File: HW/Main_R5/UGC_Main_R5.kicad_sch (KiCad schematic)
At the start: 167 parts, among them J1 SM02B-SURS-TF_LF__SN_, J10 SM02B-SURS-TF_LF__SN_, J13 503480-0640, J2 503480-0640, J4 Conn_01x06_Pin, J5 UJ31-CH-G1-SMT-TR, J6 Trigger, J7 Trigger, J8 Conn_01x02, J9 Conn_01x02, Q1 MMBT3904, Q2 MMBT3904, Q3 BSS138DW, Q4 BSS138DW, Q5 MMBT2222A, Q6 MMBT2222A, SW1 1TS026A-1000-0550, SW1 SW_Push, SW10 SW_Push, SW11 SW_Push, SW12 SW_Push, SW13 SW_Push, SW14 TS-1187A-C-A-B, SW17 TS-1187A-C-A-B, SW18 TS-1187A-C-A-B, SW19 TS-1187A-C-A-B, SW2 SW_Push, SW3 SW_Push, SW4 SW_Push, SW5 TS-1187A-C-A-B, SW6 GL18_SW, SW7 SW_Push, SW8 SW_Push, SW9 TS-1187A-C-A-B, U1 ESP32-PICO-MINI-02, U10 ST_LSM6, U11 BQ25180, U12 CH340K, U13 PI3USB4000A, U2 GD25Q80EEIGR, U4 TPS630001RCR, U5 ST_LSM6, U6 MCP3002, U7 MCP3002, U8 RP2040, X1 ModConnect, X2 ModConnect, X3 ModConnect, X4 ModConnect, X5 ModConnect, X6 ModConnect, Y1 ABM8-272-T3

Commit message: R5 Update
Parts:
- removed C2: 10uF, Capacitor_SMD:C_0805_2012Metric, symbol Device:C
- removed C20, C22: 100nF, Capacitor_SMD:C_0201_0603Metric, symbol Device:C
- removed C21: 1uF, Capacitor_SMD:C_0201_0603Metric, symbol Device:C
- removed Q1, Q2: MMBT3904, Package_TO_SOT_SMD:SOT-23, symbol Transistor_BJT:MMBT3904
- removed R20, R29, R30: 10k, Resistor_SMD:R_0201_0603Metric, symbol Device:R_Small
- removed SW1: 1TS026A-1000-0550, hhl:1TS026A-1000-0550, symbol hhl:1TS026A-1000-0550
- removed U1: ESP32-PICO-MINI-02, hhl:MODULE_ESP32-PICO-MINI-02, symbol hhl:ESP32-PICO-MINI-02
- removed U12: CH340K, hhl:ESSOP-10, symbol hhl:CH340K
- removed U13: PI3USB4000A, Package_DFN_QFN:Texas_UQFN-10_1.5x2mm_P0.5mm, symbol hhl:PI3USB4000AZUAEX
- removed U6, U7: MCP3002, Package_SO:MSOP-8_3x3mm_P0.65mm, symbol Analog_ADC:MCP3002
- added L14, L15, L8, L9: SK6805-EC-15, hhl:SK6805-EC-15, symbol progcc_v3:SK6805-EC-15
- added L7: BLM18AG601SN1D, Inductor_SMD:L_0603_1608Metric, symbol Device:L
- added P1: RPI-RM2, hhl:RPI_RM2, symbol hhl:RPI-RM2
- added S7: TMUX1204DQAR, hhl:TMUX1204DQAR, symbol hhl:TMUX1204DQAR
- added U1, U2, U3: USBLC6-2P6, Package_TO_SOT_SMD:SOT-666, symbol Power_Protection:USBLC6-2P6
- C18: footprint Capacitor_SMD:C_0201_0603Metric -> Capacitor_SMD:C_0402_1005Metric; Confirmed YES -> (none); LCSC C160831 -> C541406; Link https://www.lcsc.com/product-detail/Multilayer-Ceramic-Capa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 -> (none); MPN CL03A104KQ3NNNC -> CC0402KRX7R5BB104; Package 0201 -> 0402
- R16: Confirmed YES -> (none); Link https://www.lcsc.com/product-detail/Chip-Resistor-Surface-M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 -> (none); USBDNP (none) -> YES
- R17: value 10k -> 470R; Confirmed YES -> (none); LCSC C106225 -> C226558; Link https://www.lcsc.com/product-detail/Chip-Resistor-Surface-M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 -> (none); MPN RC0201FR-0710KL -> AC0201FR-07470RL; USBDNP (none) -> YES
- R18, R19: value 0R -> 1k; Confirmed YES -> (none); LCSC C106227 -> C138165; Link https://www.lcsc.com/product-detail/Chip-Resistor-Surface-M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 -> (none); MPN RC0201FR-070RL -> RC0201FR-071KL; Price 0.0005 -> 0.0006
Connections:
- net ESP_IO13 is gone; now on net +3V3: R19.2
- net ESP_IO15 is gone; now on net +3V3: R18.1
- net RADC_CS is gone; now on net LRA_R: U8.12 (GPIO9)
- net USB_EN is gone; now on net I2C0_SDA: U8.36 (GPIO24)
- net USB_SEL is gone; now on net I2C0_SCL: U8.37 (GPIO25)
- net +3V3: now also U10.1 (SDO), U10.12 (CS), U5.12 (CS), L14.2 (VDD), L15.2 (VDD), L7.1, L8.2 (VDD), L9.2 (VDD), S7.5 (EN), S7.6 (VDD)
- net BTN_PWR: now also U8.2 (GPIO0); no longer U8.7 (GPIO5)
- net D+: now also U1.3 (I/O2)
- net D-: now also U1.1 (I/O1)
- net GND: now also U5.1 (SDO), L14.4 (GND), L15.4 (GND), L8.4 (GND), L9.4 (GND), P1.A1 (GND), P1.A4 (GND), P1.A7 (GND), P1.B4 (GND), P1.C1 (GND), P1.C7 (GND), S7.3 (GND), U1.2 (GND), U2.2 (GND), U3.2 (GND)
- net I2C_SCL: no longer R8.2, U8.35 (GPIO23)
- net I2C_SDA: no longer R9.1, U8.34 (GPIO22)
- net LRA_L: now also U8.11 (GPIO8); no longer U8.5 (GPIO3)
- net LRA_R: no longer U8.11 (GPIO8)
- net LX: now also S7.4 (S3)
- net LY: now also S7.2 (S1)
- net N_CLOCK: now also U2.4 (I/O2); no longer Q4.6 (D1), R27.2
- net N_DATA: now also U3.6 (I/O1); no longer Q4.4 (S2), R28.2
- net N_LATCH: now also U2.6 (I/O1); no longer Q3.4 (S2), R26.2
- net RX: now also S7.7 (S4)
- net RY: now also S7.9 (S2)
- net WL_D: now reaches R16.2
- net WL_D: now also R17.1, U8.5 (GPIO3), P1.A5 (DI)
- net ESP_CTS renamed I2C0_SCL
- net I2C0_SCL: now also U10.13 (SCL), U5.13 (SCL)
- net ESP_DTR: no longer names the net of R16.1
- net ESP_DTR: now also P1.B3 (IRQ)
- net ESP_EN renamed ADC_MUX_OUT
- net ADC_MUX_OUT: now also S7.8 (D)
- net ESP_RTS: no longer names the net of R17.2
- net ESP_RTS: now also P1.A6 (DO); no longer R19.1
- removed net IMU0_CS: U10.12 (CS), U8.2 (GPIO0)
- net IMU1_CS renamed WL_ON
- net WL_ON: now also P1.B5 (WLON), P1.B6 (BTON); no longer U5.12 (CS)
- net LADC_CS: no longer names the net of U8.3 (GPIO1)
- net PLAYER_RGB: no longer names the net of L6.1 (DIN)
- net PLAYER_RGB: now also L15.3 (DOUT); no longer L4.3 (DOUT)
- net RP_USB+ renamed SAFE_D+
- net SAFE_D+: now also U1.4 (I/O2)
- net RP_USB- renamed SAFE_D-
- net SAFE_D-: now also U1.6 (I/O1)
- removed net SPI_CK: U10.13 (SCL), U5.13 (SCL), U8.8 (GPIO6)
- removed net SPI_RX: U10.1 (SDO), U5.1 (SDO), U8.6 (GPIO4)
- net SPI_TX renamed I2C0_SDA
- net I2C0_SDA: now also R19.1; no longer U8.9 (GPIO7)
- new net: L8.3 (DOUT), L9.1 (DIN)
- new net: L14.3 (DOUT), L15.1 (DIN)
- new net: L14.1 (DIN), L9.3 (DOUT)
- new net +3.3V_PRE: U3.5 (VBUS)
- new net ADC_ADDR_0: S7.1 (A0)
- new net ADC_ADDR_1: S7.10 (A1)
- new net DPAD_RGB: L4.3 (DOUT), L8.1 (DIN)
- new net I2C1_SCL: R8.2, U8.35 (GPIO23)
- new net I2C1_SDA: R9.1, U8.34 (GPIO22)
- new net N_CLOCK_SAFE: Q4.6 (D1), R27.2, U2.3 (I/O2)
- new net N_DATA_SAFE: Q4.4 (S2), R28.2, U3.1 (I/O1)
- new net N_LATCH_SAFE: Q3.4 (S2), R26.2, U2.1 (I/O1)
- new net VBUS_PRE: U1.5 (VBUS)
- new net VDDBAT: L7.2, P1.B7 (VDDIO), P1.C2 (VDDBAT)
- new net WL_CLK: P1.A3 (SCLK), U8.6 (GPIO4)
- new net WL_CS: P1.B2 (CS), U8.7 (GPIO5)
- new net WL_GP0: P1.B1 (GPIO0)
- new net WL_GP1: P1.C4 (GPIO1)
- new net WL_GP2: P1.C3 (GPIO2)
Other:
- note added: "Analog Mux"
- note added: "ESD"
- note added: "RPI-RM2 Wireless"
- note removed: "ADCs"
- note removed: "ESP32 EN Pullup"
- note removed: "ESP32 Pico Mini 02"
- note removed: "ESP32 UART Bridge IC"
- note removed: "USB Switch"
- moved on the sheet: C1, C12, C13, C2, J13, J4, L10, L11, L12, L13, L6, R1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

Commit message: More routing
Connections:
- net +3.3V_PRE is gone; now on net +3V3_PRE: U3.5 (VBUS)
- net I2C_SCL is gone; now on net I2C1_SCL: U11.B1 (SCL)
- net I2C_SDA is gone; now on net I2C1_SDA: U11.C1 (SDA)
- net VBUS_PRE is gone; now on net +5V_PRE: U1.5 (VBUS)
- net ADC_ADDR_0: now also U8.6 (GPIO4)
- net ADC_ADDR_1: now also U8.7 (GPIO5)
- net ADC_MUX_OUT: now also U8.41 (GPIO29_ADC3); no longer U8.38 (GPIO26_ADC0)
- net BTN_PWR: now also U8.8 (GPIO6); no longer U8.2 (GPIO0)
- net N_CLOCK: now also U2.6 (I/O1); no longer U2.4 (I/O2)
- net N_CLOCK_SAFE: now also U2.1 (I/O1); no longer U2.3 (I/O2)
- net N_DATA: now also U3.4 (I/O2); no longer U3.6 (I/O1)
- net N_DATA_3.3: now also Q3.3 (D2), R23.2, U8.30 (GPIO19); no longer Q4.3 (D2), R25.2, U8.31 (GPIO20)
- net N_DATA_SAFE: now also Q3.4 (S2), R26.2, U3.3 (I/O2); no longer Q4.4 (S2), R28.2, U3.1 (I/O1)
- net N_LATCH: now also U2.4 (I/O2); no longer U2.6 (I/O1)
- net N_LATCH_3.3: now also Q4.3 (D2), R25.2, U8.31 (GPIO20); no longer Q3.3 (D2), R23.2, U8.30 (GPIO19)
- net N_LATCH_SAFE: now also Q4.4 (S2), R28.2, U2.3 (I/O2); no longer Q3.4 (S2), R26.2, U2.1 (I/O1)
- net RGB_OUT: now also U8.40 (GPIO28_ADC2); no longer U8.39 (GPIO27_ADC1)
- net WL_CLK: now also U8.4 (GPIO2); no longer U8.6 (GPIO4)
- net WL_CS: now also U8.5 (GPIO3); no longer U8.7 (GPIO5)
- net WL_D: now also U8.3 (GPIO1); no longer U8.5 (GPIO3)
- net WL_ON: now also U8.2 (GPIO0); no longer U8.4 (GPIO2)
- net ZL_ANALOG: now also U8.39 (GPIO27_ADC1); no longer U8.41 (GPIO29_ADC3)
- net ZR_ANALOG: now also U8.38 (GPIO26_ADC0); no longer U8.40 (GPIO28_ADC2)
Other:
- title: GC Ultimate R4K -> GC Ultimate R5

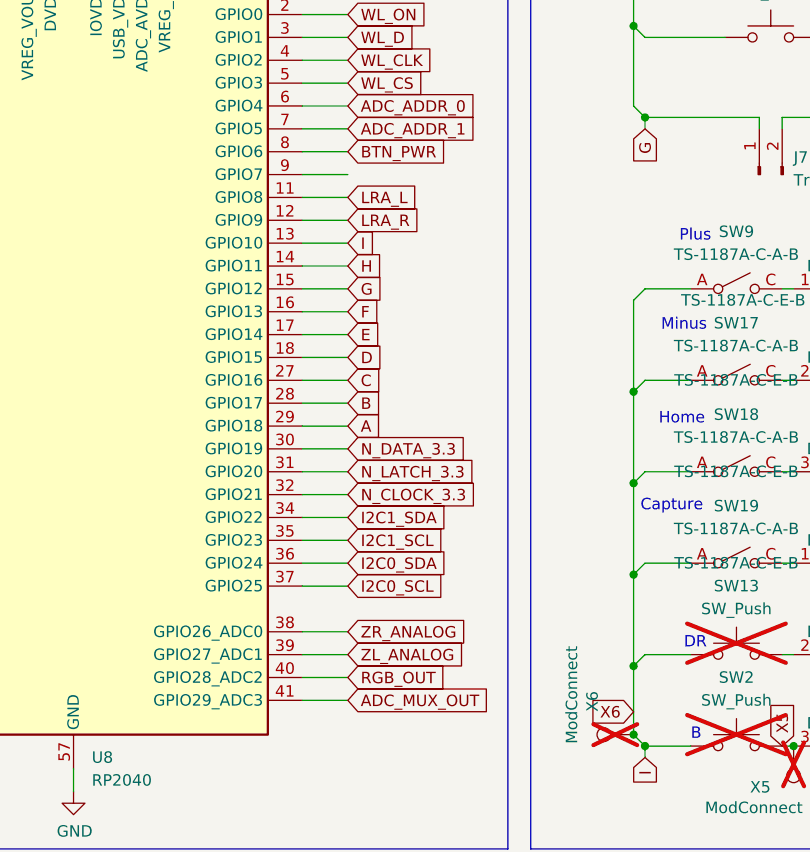
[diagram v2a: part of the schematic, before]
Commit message: Add BATLVL
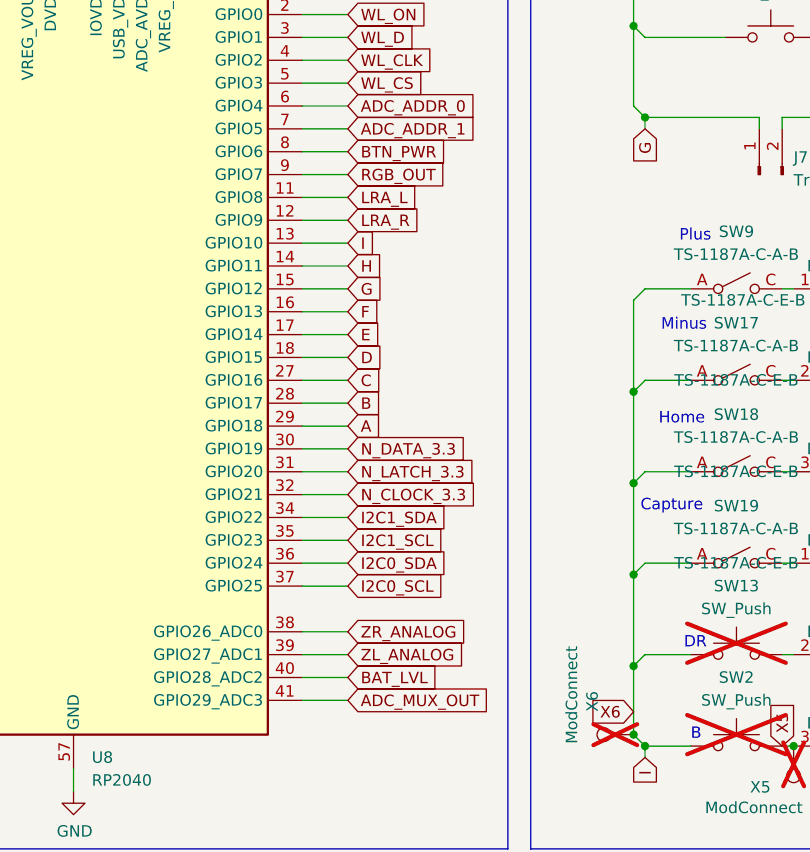
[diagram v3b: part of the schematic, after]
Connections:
- net BAT_LVL: now also U8.40 (GPIO28_ADC2)
- net RGB_OUT: now also U8.9 (GPIO7); no longer U8.40 (GPIO28_ADC2)
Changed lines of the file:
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@@
 		)
 	)
+	(global_label "BAT_LVL"
+		(shape input)
+		(at 355.6 351.79 0)
+		(fields_autoplaced yes)
+		(effects
+			(font
+				(size 1.27 1.27)
+			)
+			(justify left)
+		)
+		(property "Intersheetrefs" "${INTERSHEET_REFS}"
+			(at 365.3696 351.79 0)
+			(effects
+				(font
+					(size 1.27 1.27)
+				)
+				(justify left)
+				(hide yes)
+			)
+		)
+	)
 	(global_label "F"
 		(shape input)
@@
 		)
 	)
-	(global_label "RGB_OUT"
-		(shape input)
-		(at 355.6 351.79 0)
-		(fields_autoplaced yes)
-		(effects
-			(font
-				(size 1.27 1.27)
-			)
-			(justify left)
-		)
-		(property "Intersheetrefs" "${INTERSHEET_REFS}"
-			(at 366.3304 351.7106 0)
-			(effects
-				(font
-					(size 1.27 1.27)
-				)
-				(justify left)
-				(hide yes)
-			)
-		)
-	)
 	(global_label "X6"
 		(shape input)
@@
 				(hide yes)
 			)
+		)
+	)
+	(global_label "RGB_OUT"
+		(shape input)
+		(at 355.6 295.91 0)
+		(fields_autoplaced yes)
+		(effects
+			(font
+				(size 1.27 1.27)
+			)
+			(justify left)
+		)
+		(property "Intersheetrefs" "${INTERSHEET_REFS}"
+			(at 366.3304 295.8306 0)
+			(effects
+				(font
+					(size 1.27 1.27)
+				)
+				(justify left)
+				(hide yes)
+			)
